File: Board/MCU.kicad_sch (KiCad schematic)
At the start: 27 parts, among them J1 Conn_01x06_Male, SW1 RST_BTN, SW2 SCREEN_OFF_BTN, U1 ESP32-WROOM-32

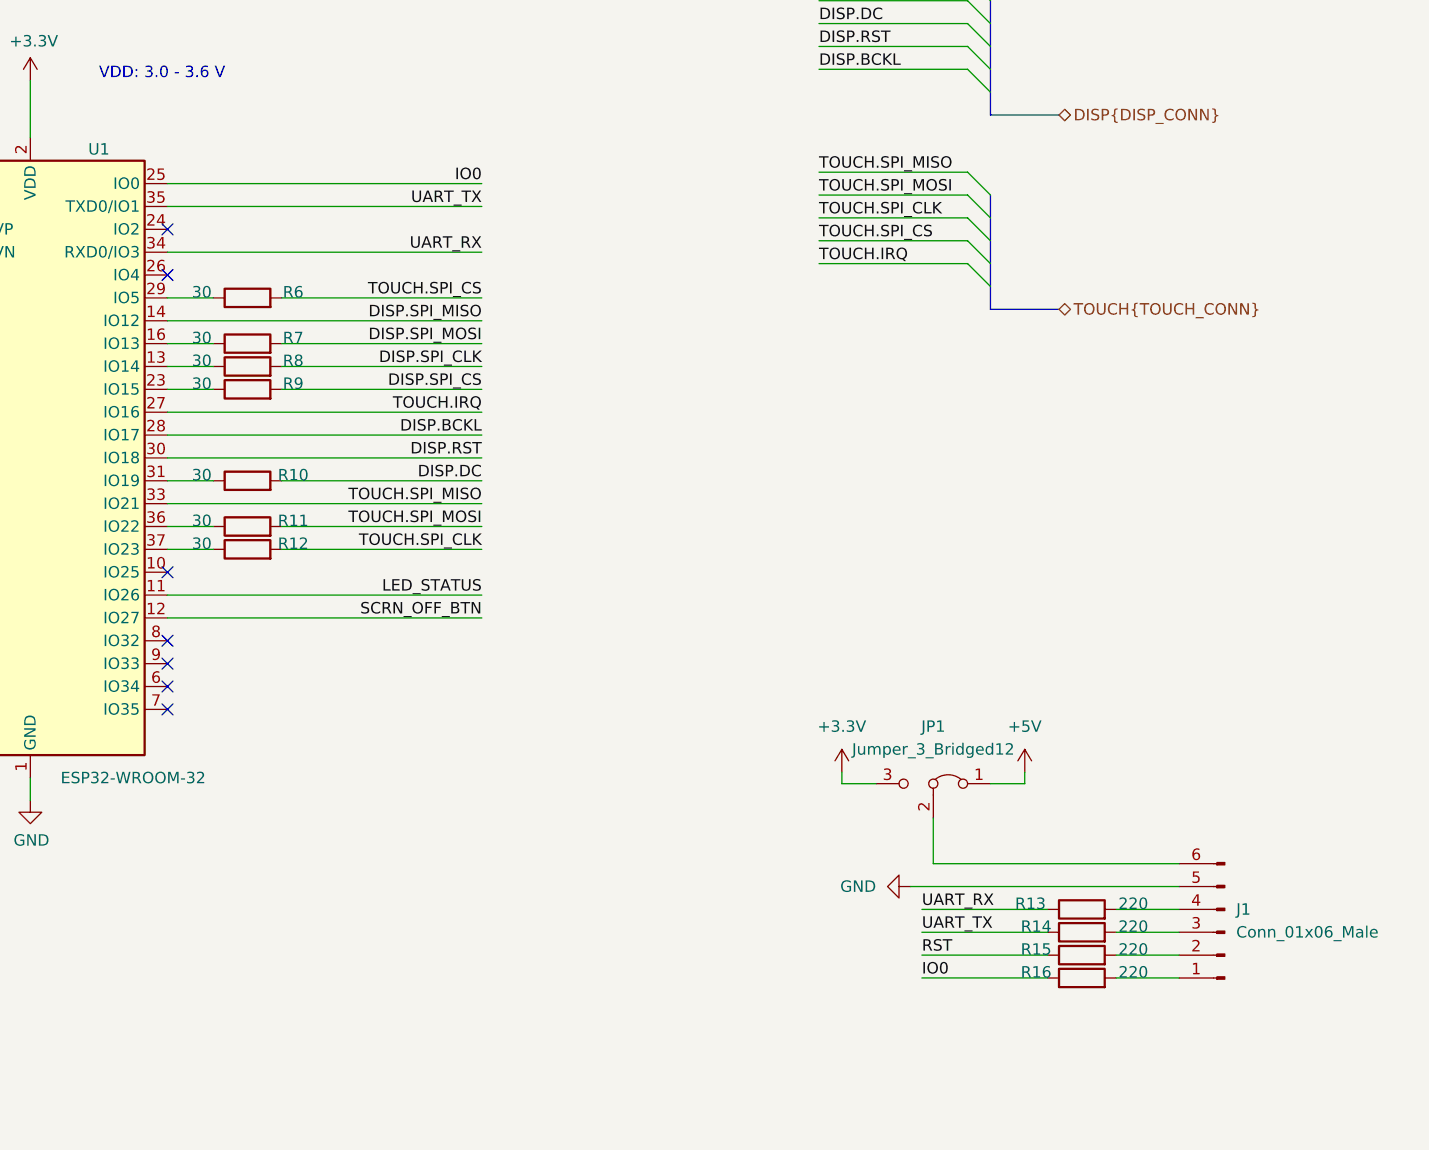
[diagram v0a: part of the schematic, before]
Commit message: Add I2C pin header
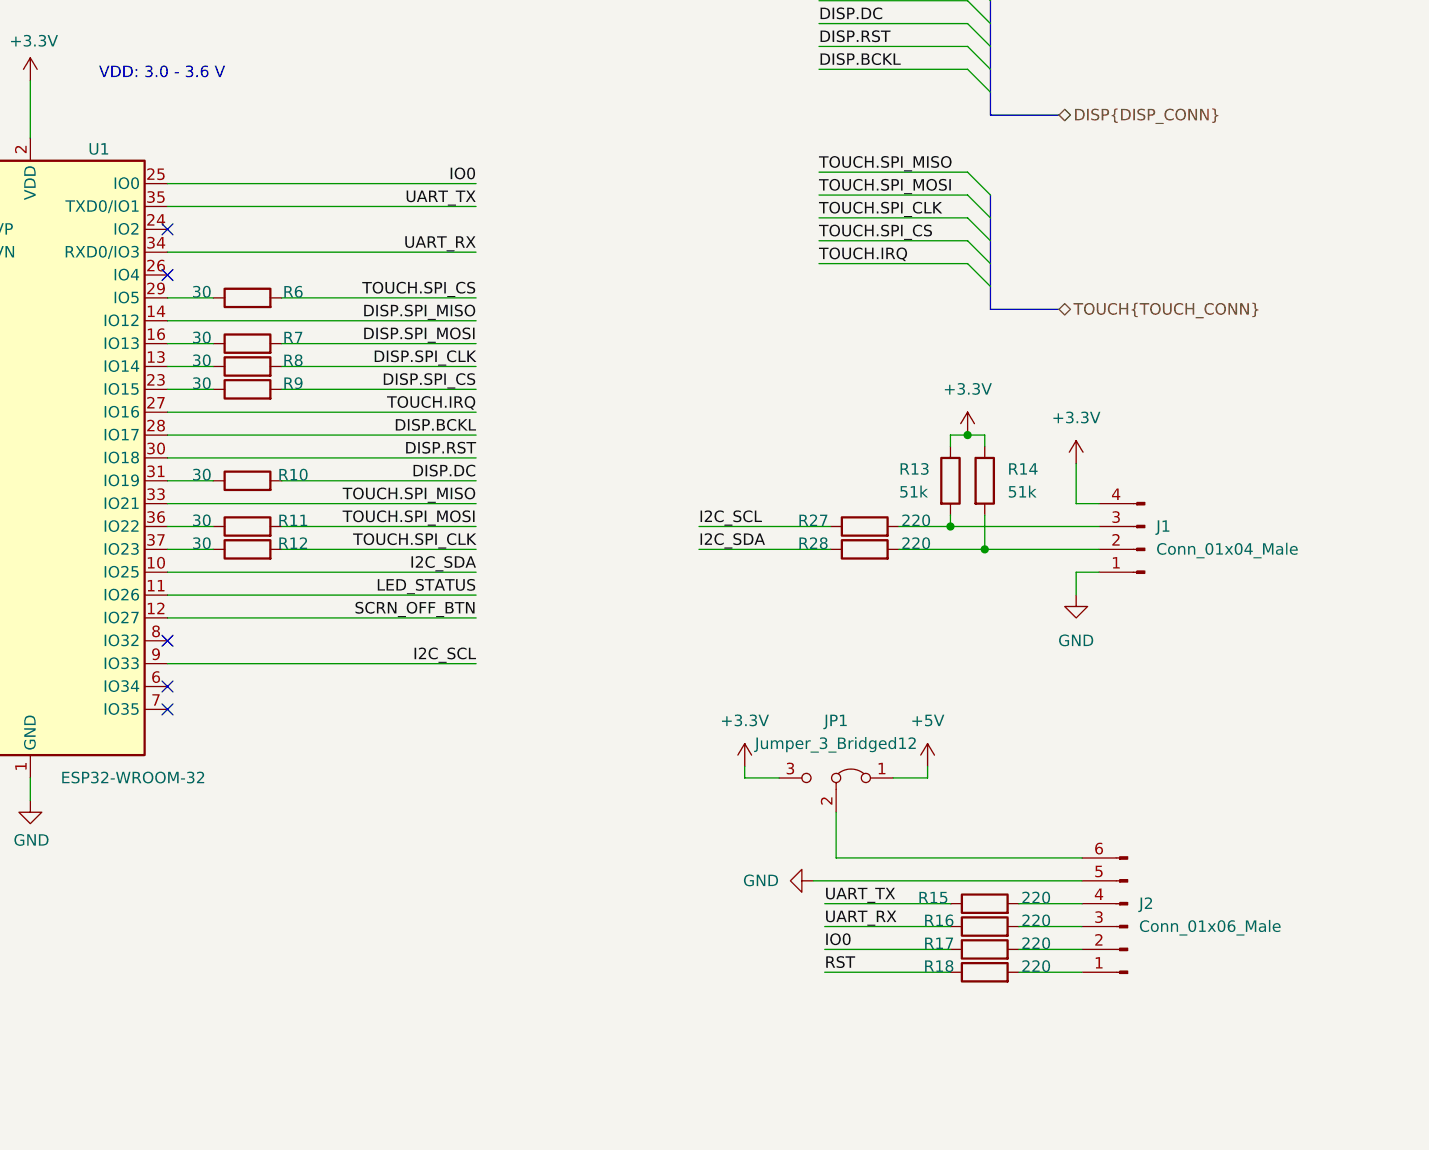
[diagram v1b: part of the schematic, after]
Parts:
- added J1: Conn_01x04_Male, Connector_PinHeader_2.54mm:PinHeader_1x04_P2.54mm_Horizontal, symbol Connector:Conn_01x04_Male
- added R13, R14: 51k, Resistor_SMD:R_0603_1608Metric_Pad0.98x0.95mm_HandSolder, symbol Device:R
- added R27, R28: 220, Resistor_SMD:R_0603_1608Metric_Pad0.98x0.95mm_HandSolder, symbol Device:R
- renumbered J1 to J2, R13 to R15, R14 to R16, R15 to R17, R16 to R18
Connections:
- net +3V3: now also J1.4 (Pin_4), R13.1, R14.1
- net GND: now also J1.1 (Pin_1)
- net IO0: now also R17.1; no longer R18.1
- net RST: now also R18.1; no longer R17.1
- net UART_RX: now also R16.1; no longer R15.1
- net UART_TX: now also R15.1; no longer R16.1
- net I2C_SDA: now reaches U1.10 (IO25)
- net I2C_SDA: now also R28.1
- net I2C_SCL: now reaches U1.9 (IO33)
- net I2C_SCL: now also R27.1
- new net: J1.2 (Pin_2), R14.2, R28.2
- new net: J1.3 (Pin_3), R13.2, R27.2
- no-connect marks 15 -> 13
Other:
- moved on the sheet: J2, JP1, R15, R16, R17, R18

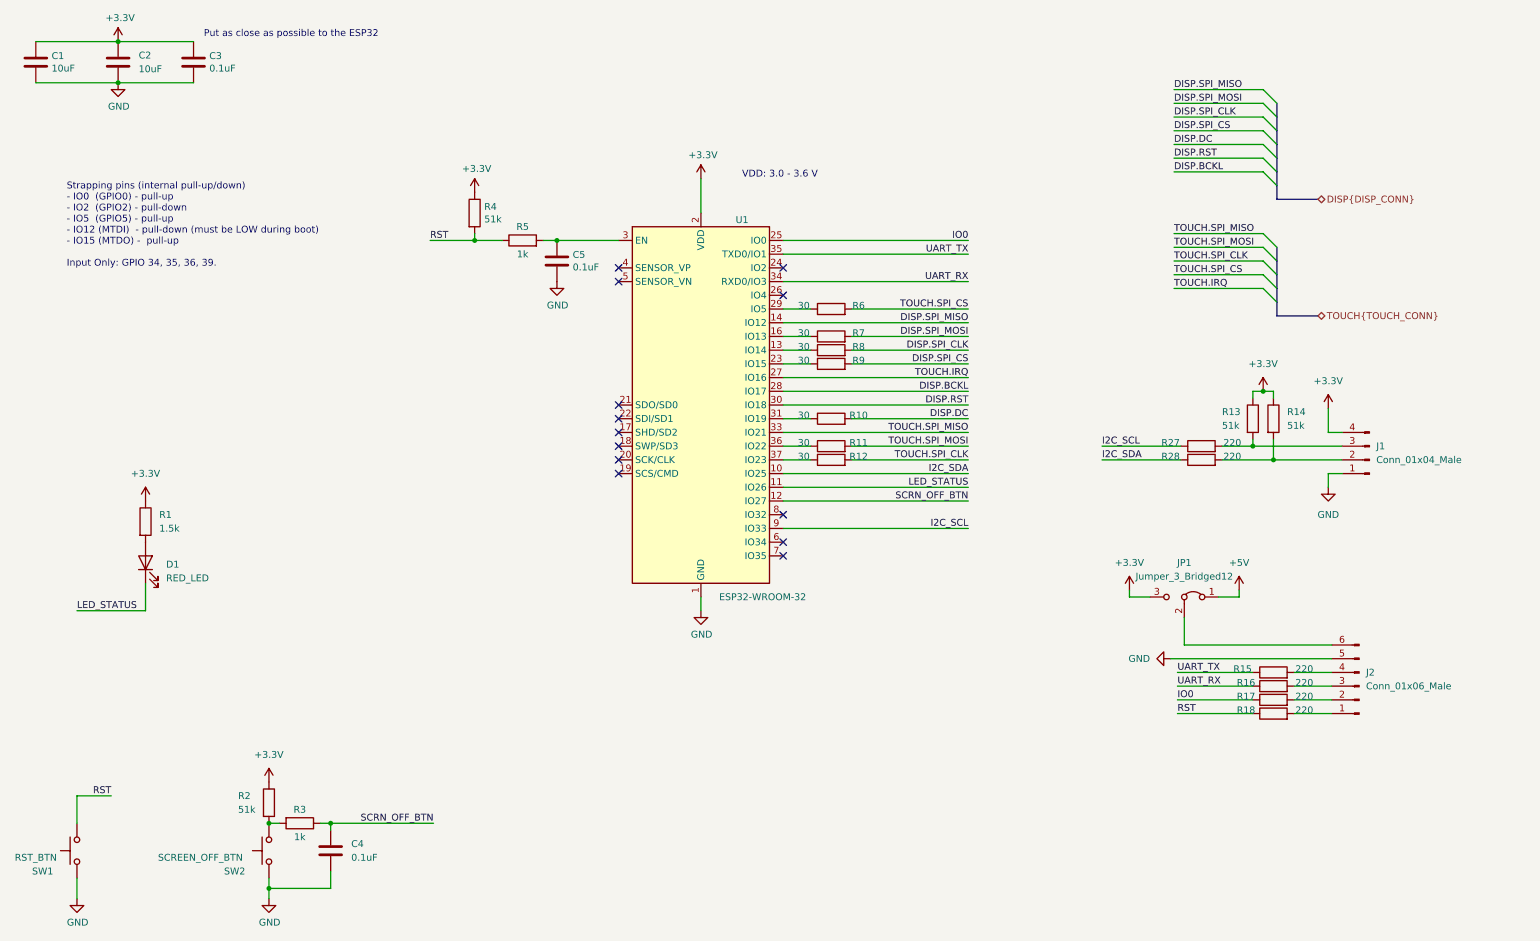
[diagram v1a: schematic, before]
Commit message: Fix USB silkscreen over board warning, other minimal fixes
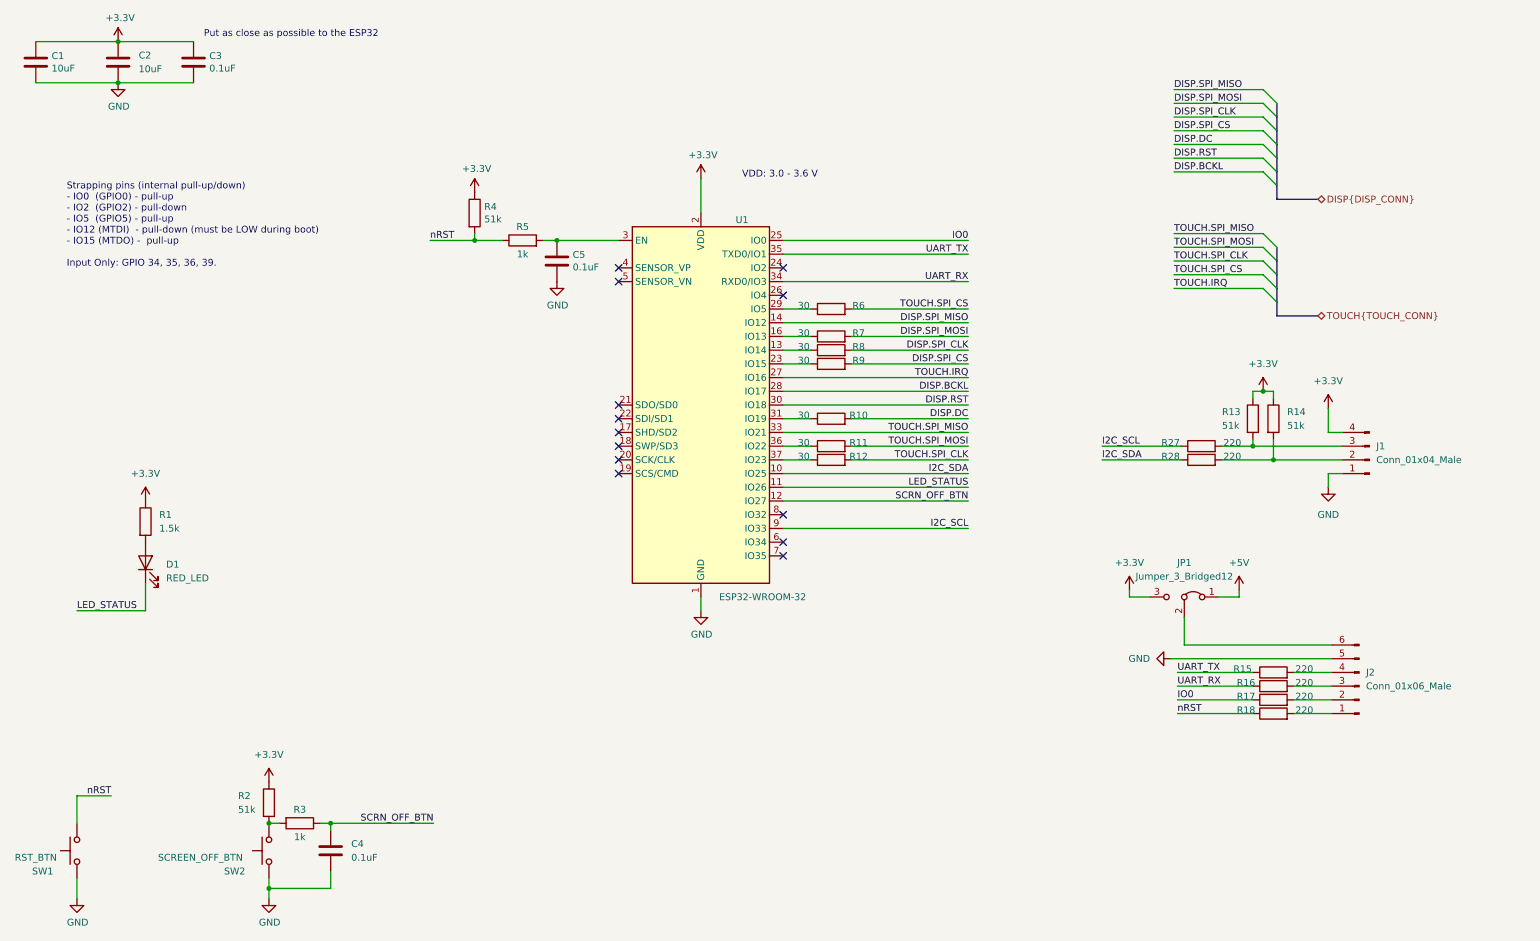
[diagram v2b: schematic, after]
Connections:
- net RST renamed nRST
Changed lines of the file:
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@@
   (title_block
     (title "MCU")
-    (date "2022/01/12")
+    (date "2022/01/17")
     (rev "v0.1")
     (company "Bzgec")
@@
     (effects (font (size 1.27 1.27)) (justify right bottom))
   )
-  (label "RST" (at 31.75 162.56 180)
+  (label "nRST" (at 31.75 162.56 180)
     (effects (font (size 1.27 1.27)) (justify right bottom))
   )
@@
     (effects (font (size 1.27 1.27)) (justify left bottom))
   )
-  (label "RST" (at 229.235 147.32 0)
+  (label "nRST" (at 229.235 147.32 0)
     (effects (font (size 1.27 1.27)) (justify left bottom))
   )
@@
     (effects (font (size 1.27 1.27)) (justify right bottom))
   )
-  (label "RST" (at 90.805 59.69 0)
-    (effects (font (size 1.27 1.27)) (justify left bottom))
-  )
+  (label "nRST" (at 90.805 59.69 0)
+    (effects (font (size 1.27 1.27)) (justify left bottom))
+  )

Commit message: Add fiducials
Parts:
- renumbered J2 to J1, J1 to J2, R27 to R13, R28 to R14, R13 to R15, R14 to R16, R15 to R17, R16 to R18, R17 to R19, R18 to R20
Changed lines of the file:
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@@
   (title_block
     (title "MCU")
-    (date "2022/01/17")
+    (date "2022/01/18")
     (rev "v0.1")
     (company "Bzgec")
@@
   (symbol (lib_id "Device:R") (at 247.015 144.78 90) (unit 1)
     (in_bom yes) (on_board yes)
-    (property "Reference" "R17" (id 0) (at 241.935 144.145 90))
+    (property "Reference" "R19" (id 0) (at 241.935 144.145 90))
     (property "Value" "220" (id 1) (at 252.73 144.145 90))
     (property "Footprint" "Resistor_SMD:R_0603_1608Metric_Pad0.98x0.95mm_HandSolder" (id 2) (at 247.015 146.558 90)
@@
   (symbol (lib_id "Device:R") (at 233.68 100.33 90) (unit 1)
     (in_bom yes) (on_board yes)
-    (property "Reference" "R28" (id 0) (at 227.965 99.695 90))
+    (property "Reference" "R14" (id 0) (at 227.965 99.695 90))
     (property "Value" "220" (id 1) (at 239.395 99.695 90))
     (property "Footprint" "Resistor_SMD:R_0603_1608Metric_Pad0.98x0.95mm_HandSolder" (id 2) (at 233.68 102.108 90)
@@
   (symbol (lib_id "Connector:Conn_01x06_Male") (at 262.89 142.24 180) (unit 1)
     (in_bom yes) (on_board yes) (fields_autoplaced)
-    (property "Reference" "J2" (id 0) (at 264.16 139.6999 0)
+    (property "Reference" "J1" (id 0) (at 264.16 139.6999 0)
       (effects (font (size 1.27 1.27)) (justify right))
     )
@@
   (symbol (lib_id "Device:R") (at 243.205 92.71 0) (unit 1)
     (in_bom yes) (on_board yes)
-    (property "Reference" "R13" (id 0) (at 237.49 91.44 0)
+    (property "Reference" "R15" (id 0) (at 237.49 91.44 0)
       (effects (font (size 1.27 1.27)) (justify left))
     )
@@
   (symbol (lib_id "Device:R") (at 247.015 147.32 90) (unit 1)
     (in_bom yes) (on_board yes)
-    (property "Reference" "R18" (id 0) (at 241.935 146.685 90))
+    (property "Reference" "R20" (id 0) (at 241.935 146.685 90))
     (property "Value" "220" (id 1) (at 252.73 146.685 90))
     (property "Footprint" "Resistor_SMD:R_0603_1608Metric_Pad0.98x0.95mm_HandSolder" (id 2) (at 247.015 149.098 90)
@@
   (symbol (lib_id "Device:R") (at 247.015 142.24 90) (unit 1)
     (in_bom yes) (on_board yes)
-    (property "Reference" "R16" (id 0) (at 241.935 141.605 90))
+    (property "Reference" "R18" (id 0) (at 241.935 141.605 90))
     (property "Value" "220" (id 1) (at 252.73 141.605 90))
     (property "Footprint" "Resistor_SMD:R_0603_1608Metric_Pad0.98x0.95mm_HandSolder" (id 2) (at 247.015 144.018 90)
@@
   (symbol (lib_id "Connector:Conn_01x04_Male") (at 264.795 100.33 180) (unit 1)
     (in_bom yes) (on_board yes) (fields_autoplaced)
-    (property "Reference" "J1" (id 0) (at 266.065 97.7899 0)
+    (property "Reference" "J2" (id 0) (at 266.065 97.7899 0)
       (effects (font (size 1.27 1.27)) (justify right))
     )
@@
   (symbol (lib_id "Device:R") (at 247.015 139.7 90) (unit 1)
     (in_bom yes) (on_board yes)
-    (property "Reference" "R15" (id 0) (at 241.3 139.065 90))
+    (property "Reference" "R17" (id 0) (at 241.3 139.065 90))
     (property "Value" "220" (id 1) (at 252.73 139.065 90))
     (property "Footprint" "Resistor_SMD:R_0603_1608Metric_Pad0.98x0.95mm_HandSolder" (id 2) (at 247.015 141.478 90)
@@
   (symbol (lib_id "Device:R") (at 247.015 92.71 0) (unit 1)
     (in_bom yes) (on_board yes) (fields_autoplaced)
-    (property "Reference" "R14" (id 0) (at 249.555 91.4399 0)
+    (property "Reference" "R16" (id 0) (at 249.555 91.4399 0)
       (effects (font (size 1.27 1.27)) (justify left))
     )
@@
   (symbol (lib_id "power:+3.3V") (at 245.11 87.63 0) (unit 1)
     (in_bom yes) (on_board yes) (fields_autoplaced)
-    (property "Reference" "#PWR0101" (id 0) (at 245.11 91.44 0)
+    (property "Reference" "#PWR014" (id 0) (at 245.11 91.44 0)
       (effects (font (size 1.27 1.27)) hide)
     )
@@
   (symbol (lib_id "Device:R") (at 233.68 97.79 90) (unit 1)
     (in_bom yes) (on_board yes)
-    (property "Reference" "R27" (id 0) (at 227.965 97.155 90))
+    (property "Reference" "R13" (id 0) (at 227.965 97.155 90))
     (property "Value" "220" (id 1) (at 239.395 97.155 90))
     (property "Footprint" "Resistor_SMD:R_0603_1608Metric_Pad0.98x0.95mm_HandSolder" (id 2) (at 233.68 99.568 90)
